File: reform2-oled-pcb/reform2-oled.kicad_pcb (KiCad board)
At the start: 2 copper layers, 80 x 12 mm, 14 parts, among them J1 AUX, U1 SSD1306

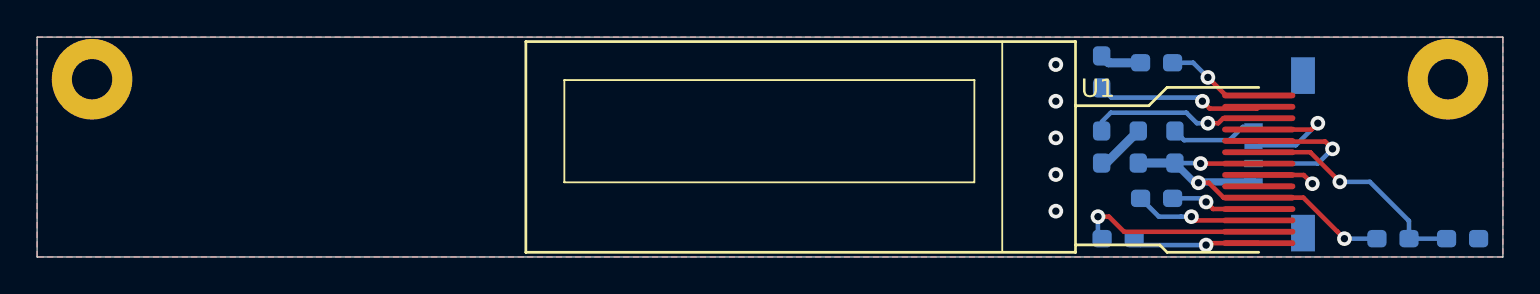
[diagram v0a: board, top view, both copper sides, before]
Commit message: reform2: update PCBs incl. badges to production revs, add keyboard lettering, misc docs
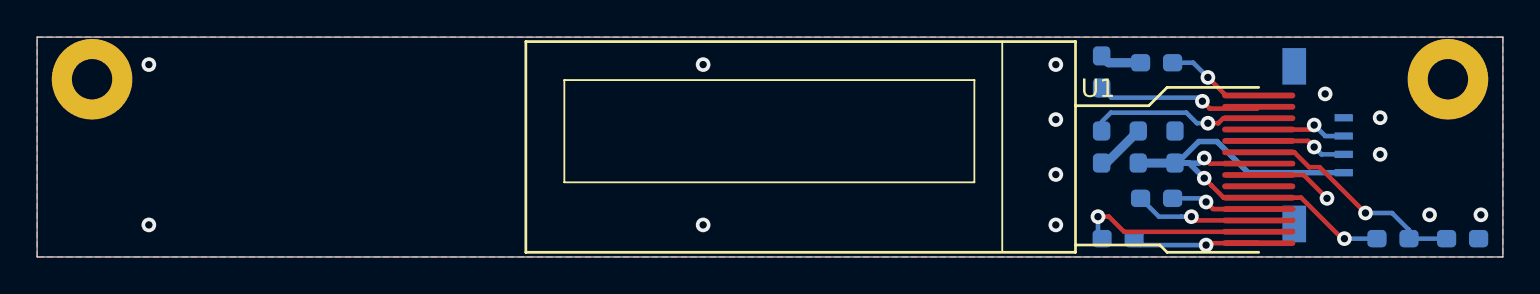
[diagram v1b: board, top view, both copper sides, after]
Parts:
- removed GFX1: MNT, reform2:mntreform
- added GFX2: BADGE, footprints-oled:reform2-oled-badge, B.Cu at (124.6, 94.4)
- moved J1 3.14 mm to (173.8, 94.4), turned to 90 degrees
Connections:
- J1 pad 1: GND -> +3V3
- J1 pad 2: DISP_SDA -> DISP_SCL
- J1 pad 3: DISP_SCL -> DISP_SDA
- J1 pad 4: +3V3 -> GND
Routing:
- net +3V3: track 22.3 -> 30.0 mm
- net DISP_SCL: track 8.85 -> 4.94 mm
- net GND: track 12.9 -> 9.26 mm, vias 6 -> 14
- net DISP_SDA: track 7.37 -> 4.99 mm
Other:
- board text removed: "REFORM OLED 2.0D-4 2020-04-19 MNTRE.COM LICENSE: CERN-OHL-S 2.0"
